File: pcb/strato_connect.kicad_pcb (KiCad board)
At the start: 2 copper layers, 39 parts, among them J1 Conn_Coaxial, J2 Conn_02x03_Odd_Even, SW1 SW_SPST, SW2 SW_SPST, U1 TPS565242, U2 ATmega328PB-A, U4 RF4463F30, Y1 CSTNE16M0V530000R0

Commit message: rough layout of the rev2 pcb
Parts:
- added J3: Conn_01x04_Pin, Connector_JST:JST_SH_SM04B-SRSS-TB_1x04-1MP_P1.00mm_Horizontal, F.Cu at (202.9, 74.3)
- added J4: Conn_01x02_Pin, Connector_JST:JST_PH_S2B-PH-SM4-TB_1x02-1MP_P2.00mm_Horizontal, F.Cu at (219.3, 72.8)
- added J5: Conn_01x05_Pin, Connector_JST:JST_SH_SM05B-SRSS-TB_1x05-1MP_P1.00mm_Horizontal, F.Cu at (203.4, 66.7)
- J2: footprint Connector_PinHeader_2.54mm:PinHeader_2x03_P2.54mm_Vertical -> Connector_PinHeader_2.54mm:PinHeader_2x03_P2.54mm_Vertical_SMD
- U2: value ATmega328PB-A -> ATmega328PB-M; footprint Package_QFP:TQFP-32_7x7mm_P0.8mm -> Package_DFN_QFN:QFN-32-1EP_5x5mm_P0.5mm_EP3.1x3.1mm
- moved U2 36.6 mm to (218.5, 79.5)

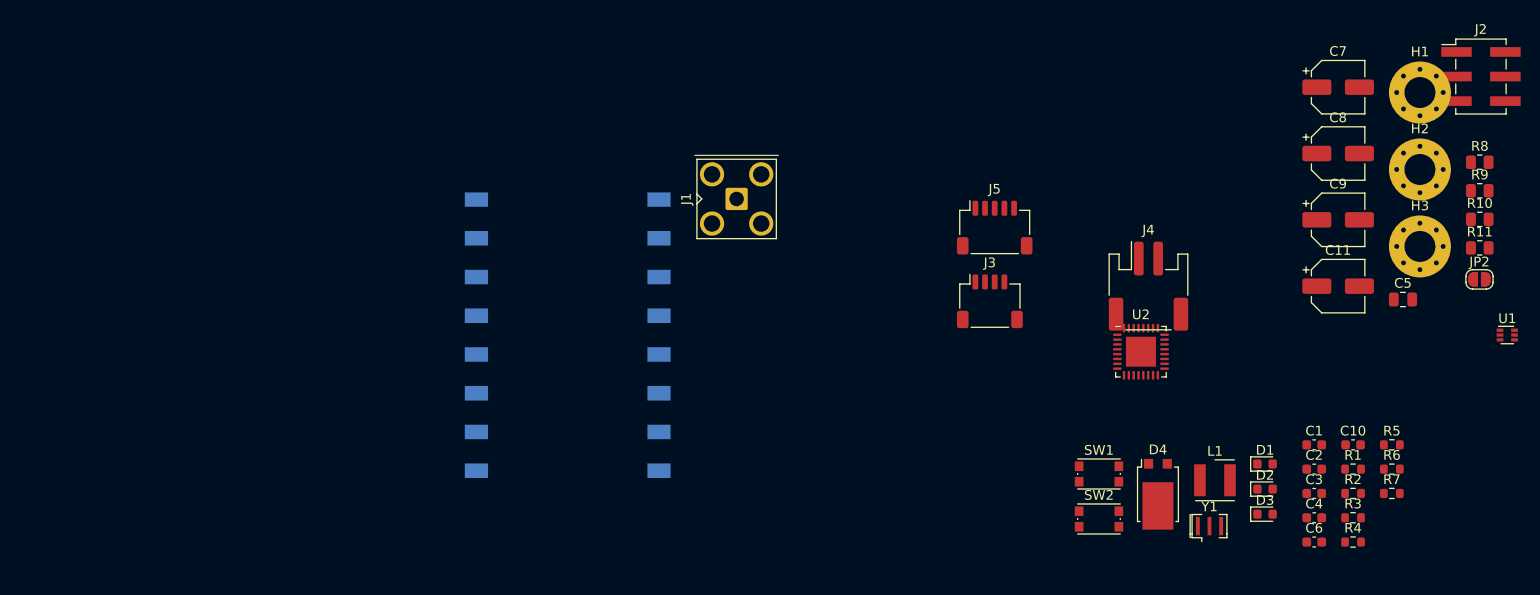
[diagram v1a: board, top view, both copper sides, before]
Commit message: get most of the layout done, need to add some sort of icsp header pins
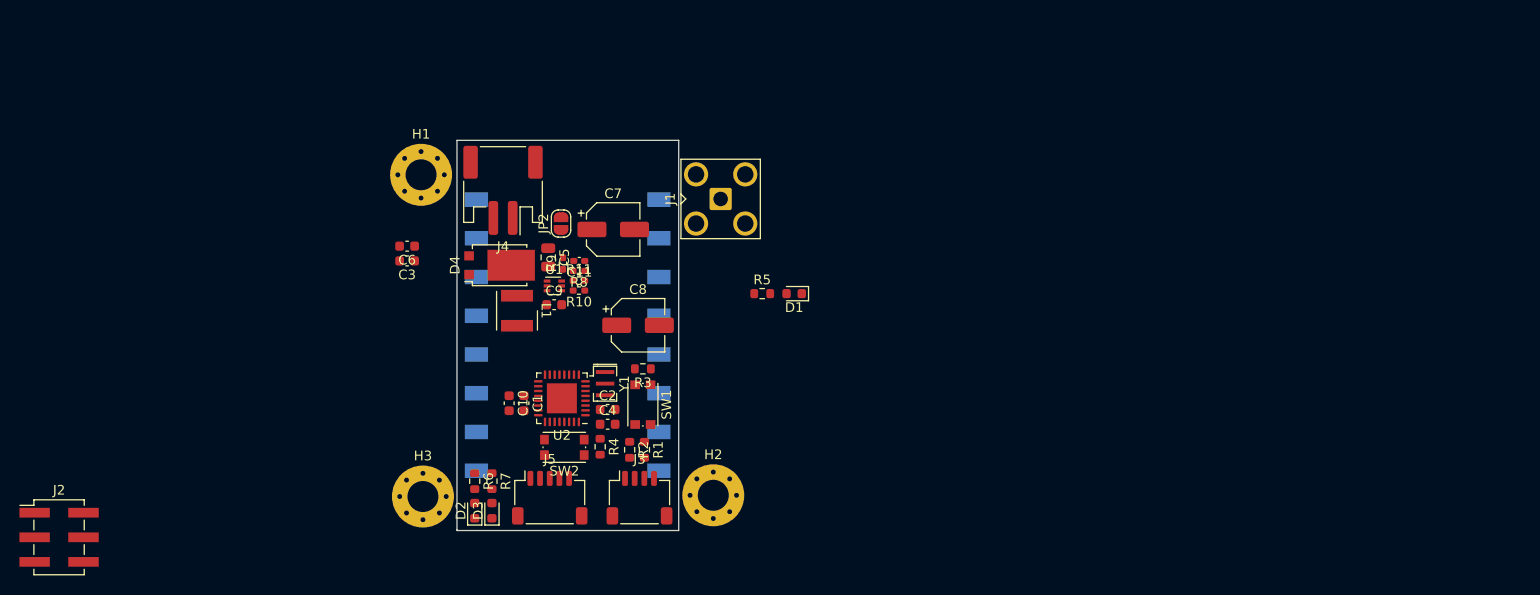
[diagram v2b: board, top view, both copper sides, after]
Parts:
- C11: footprint Capacitor_SMD:CP_Elec_5x5.3 -> Capacitor_SMD:C_0402_1005Metric_Pad0.74x0.62mm_HandSolder
- C9: footprint Capacitor_SMD:CP_Elec_5x5.3 -> Capacitor_SMD:C_0603_1608Metric
- R10, R11, R8, R9: footprint Resistor_SMD:R_0805_2012Metric -> Resistor_SMD:R_0402_1005Metric_Pad0.72x0.64mm_HandSolder
- moved J2 154.4 mm to (106.8, 98.7)
- moved H3 106.2 mm to (144.4, 94.5)
- moved H1 103.5 mm to (144.2, 61.3)
- moved U1 98.6 mm to (158.0, 72.7)
- moved C6 98.5 mm to (142.7, 68.6), turned to 180 degrees
- moved C3 96.7 mm to (142.7, 70.2), turned to 180 degrees
- moved JP2 95.0 mm to (158.6, 66.3), turned to 90 degrees
- moved R9 95.0 mm to (158.8, 70.4), turned to 90 degrees
- moved R6 94.7 mm to (149.7, 92.9), turned to -90 degrees
- moved R8 93.7 mm to (160.5, 71.2), turned to 180 degrees
- moved R10 93.3 mm to (160.5, 73.2), turned to 180 degrees
- moved R11 93.1 mm to (160.5, 72.2)
- moved R7 93.0 mm to (151.5, 92.9), turned to -90 degrees
- moved C5 88.4 mm to (157.3, 69.8), turned to -90 degrees
- moved C10 87.3 mm to (153.3, 84.9), turned to -90 degrees
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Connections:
- C5 pad 1: Net-(D4-K) -> /VDC_FW
- C9 pad 2: Net-(U1-VBST) -> GND
- D4 pad 1: Net-(D4-K) -> /VDC_FW
- R10 pad 1: Net-(D4-K) -> /VDC_FW
- U1 pad 1: GND -> /VDC_FW
- U1 pad 3: Net-(D4-K) -> GND
- U1 pad 4: /FB -> GND
- U1 pad 6: Net-(U1-VBST) -> /FB
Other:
- board outline added: 22.9 x 40.3 mm

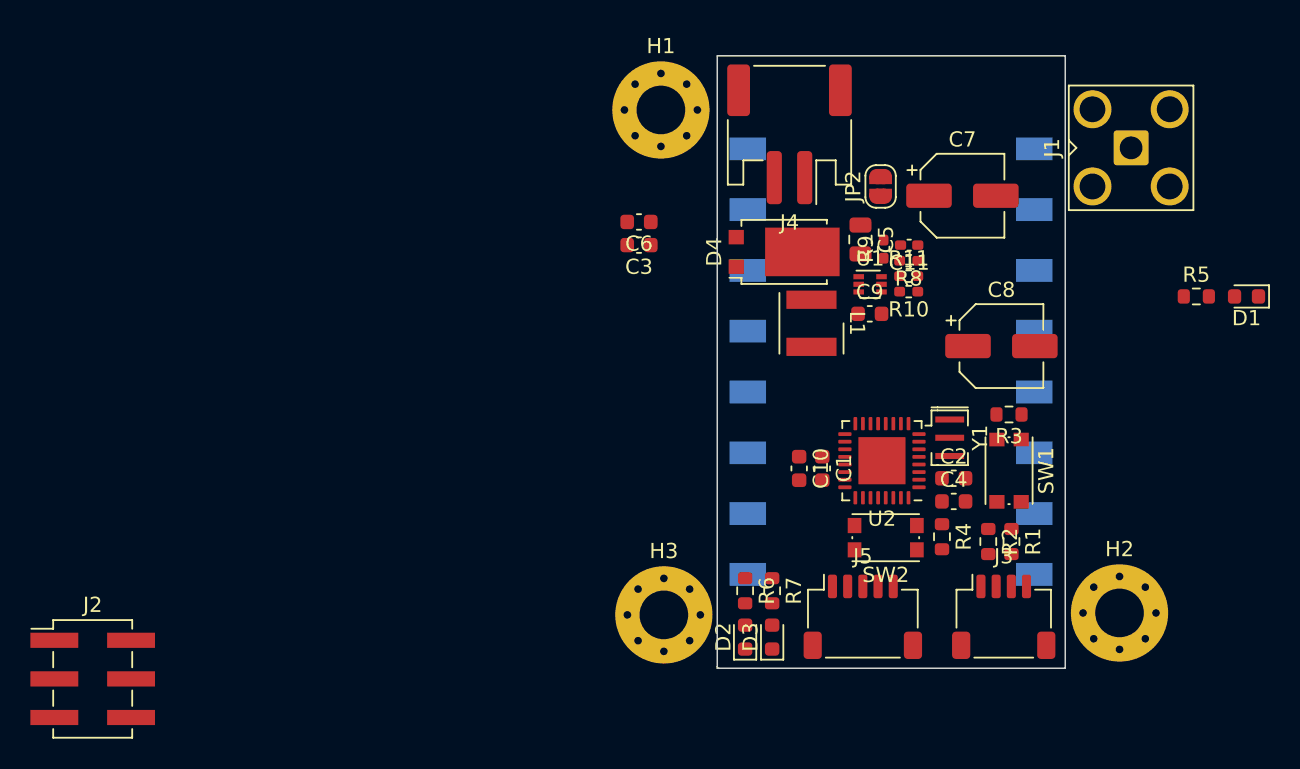
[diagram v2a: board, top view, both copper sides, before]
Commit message: pass DRC with the schematic capture
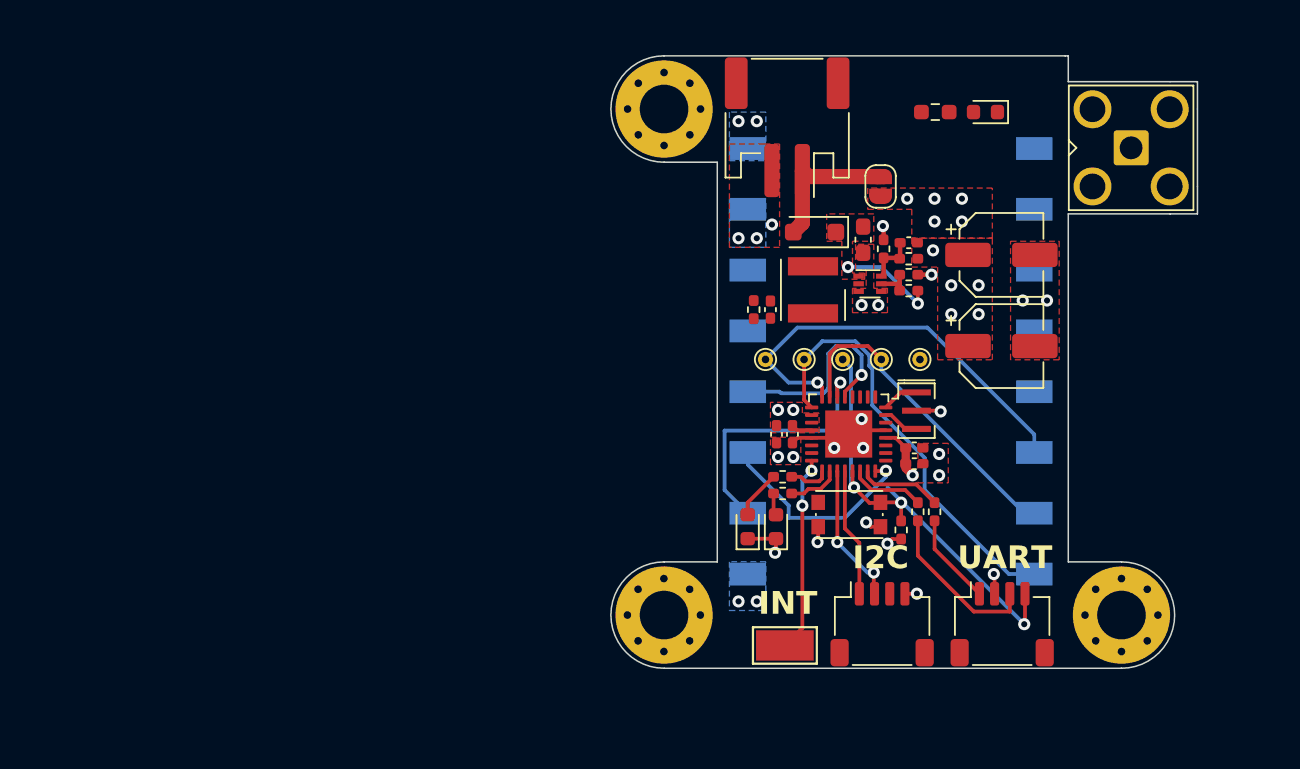
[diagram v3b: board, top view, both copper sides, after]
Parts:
- removed C3: 1u, Capacitor_SMD:C_0603_1608Metric
- removed C6: 100n, Capacitor_SMD:C_0603_1608Metric
- removed R4: 10k, Resistor_SMD:R_0603_1608Metric
- removed SW2: SW_SPST, Button_Switch_SMD:SW_Push_1P1T_NO_CK_KMR2
- added R12: NP, Resistor_SMD:R_0402_1005Metric_Pad0.72x0.64mm_HandSolder, F.Cu at (150.3, 74.4)
- added TP1: TestPoint, TestPoint:TestPoint_THTPad_D1.0mm_Drill0.5mm, F.Cu at (151.1, 77.7)
- added TP2: TestPoint, TestPoint:TestPoint_THTPad_D1.0mm_Drill0.5mm, F.Cu at (153.6, 77.7)
- added TP3: TestPoint, TestPoint:TestPoint_THTPad_D1.0mm_Drill0.5mm, F.Cu at (156.2, 77.7)
- added TP4: TestPoint, TestPoint:TestPoint_THTPad_D1.0mm_Drill0.5mm, F.Cu at (158.7, 77.7)
- added TP5: TestPoint, TestPoint:TestPoint_THTPad_D1.0mm_Drill0.5mm, F.Cu at (161.2, 77.7)
- C1, C10, C2, C4: footprint Capacitor_SMD:C_0603_1608Metric -> Capacitor_SMD:C_0402_1005Metric_Pad0.74x0.62mm_HandSolder
- C5: footprint Capacitor_SMD:C_0805_2012Metric -> Capacitor_SMD:C_0603_1608Metric_Pad1.08x0.95mm_HandSolder
- C9: value 100n -> NP; footprint Capacitor_SMD:C_0603_1608Metric -> Capacitor_SMD:C_0402_1005Metric_Pad0.74x0.62mm_HandSolder
- D4: value ST12199STR -> FS22N; footprint Kevin_Lutzer_Lbr:Diode-TO-277B -> Diode_SMD:D_SOD-123F
- J2: value Conn_02x03_Odd_Even -> Conn_01x04_Pin; footprint Connector_PinHeader_2.54mm:PinHeader_2x03_P2.54mm_Vertical_SMD -> Connector_JST:JST_SH_SM04B-SRSS-TB_1x04-1MP_P1.00mm_Horizontal
- J5: value Conn_01x05_Pin -> Conn_01x01_Pin; footprint Connector_JST:JST_SH_SM05B-SRSS-TB_1x05-1MP_P1.00mm_Horizontal -> TestPoint:TestPoint_Keystone_5019_Minature
- R1, R2, R3, R6, R7: footprint Resistor_SMD:R_0603_1608Metric -> Resistor_SMD:R_0402_1005Metric_Pad0.72x0.64mm_HandSolder
- R5: footprint Resistor_SMD:R_0603_1608Metric -> Resistor_SMD:R_0603_1608Metric_Pad0.98x0.95mm_HandSolder
- moved J2 52.1 mm to (158.8, 95.1)
- moved R5 21.0 mm to (162.2, 61.4)
- moved D1 21.0 mm to (165.6, 61.4)
- moved SW1 10.9 mm to (156.6, 87.9), turned to 180 degrees
- moved R3 10.4 mm to (160.0, 88.9), turned to 90 degrees
- moved R6 7.90 mm to (152.2, 85.4), turned to 180 degrees
- moved D3 7.27 mm to (151.8, 88.7)
- moved D2 7.26 mm to (149.9, 88.7)
- moved C9 6.54 mm to (151.4, 74.4), turned to 90 degrees
- moved R1 6.46 mm to (161.1, 87.7)
- moved R7 6.44 mm to (152.2, 86.5), turned to 180 degrees
- moved J5 5.47 mm to (152.3, 96.5), turned to 180 degrees
- moved C7 4.67 mm to (166.6, 70.8)
- moved R2 4.04 mm to (162.2, 87.7)
- moved C4 3.59 mm to (160.9, 84.5)
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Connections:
- C9 pad 1: /SW -> +5V
- C9 pad 2: GND -> /SW
- J2 pad 1: SPI_MISO -> SCL
- J2 pad 2: +5V -> SDA
- J2 pad 3: SPI_SCK -> unconnected-(J2-Pin_3-Pad3)
- J2 pad 4: SPI_MOSI -> GND
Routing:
- net ~{RST}: track 0.00 -> 29.3 mm, vias 0 -> 3
- net SPI_SCK: track 0.00 -> 28.4 mm
- net SPI_MISO: track 0.00 -> 27.8 mm, vias 0 -> 1
- net SPI_MOSI: track 0.00 -> 21.5 mm
- net ~{SPI_CS}: track 0.00 -> 17.7 mm, vias 0 -> 1
- net GND: track 0.00 -> 16.9 mm, vias 0 -> 24
- net ~{IRQ}: track 0.00 -> 14.0 mm, vias 0 -> 1
- net ~{SDN}: track 0.00 -> 13.6 mm, vias 0 -> 1
- net ~{INT}: track 0.00 -> 12.9 mm, vias 0 -> 2
- net UART_RX: track 0.00 -> 11.0 mm
- net VDC: track 0.00 -> 9.61 mm
- net SDA: track 0.00 -> 9.33 mm, vias 0 -> 2
- net SCL: track 0.00 -> 8.47 mm
- net /VDC_FW: track 0.00 -> 6.45 mm, vias 0 -> 2
- net UART_TX: track 0.00 -> 6.02 mm
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- added copper zone on B.Cu, net +5V
- added copper zone on F.Cu, net +5V
- added copper zone on In1.Cu, net +5V
- added copper zone on F.Cu, net /VDC_FW
- added copper zone on B.Cu, net GND
- added copper zone on F.Cu, net GND
- added copper zone on In2.Cu, net GND
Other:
- board size 22.9 x 40.3 mm -> 38.6 x 40.3 mm
- copper layers 2 -> 4
- board text added: "I2C"
- board text added: "INT"
- board text added: "UART"

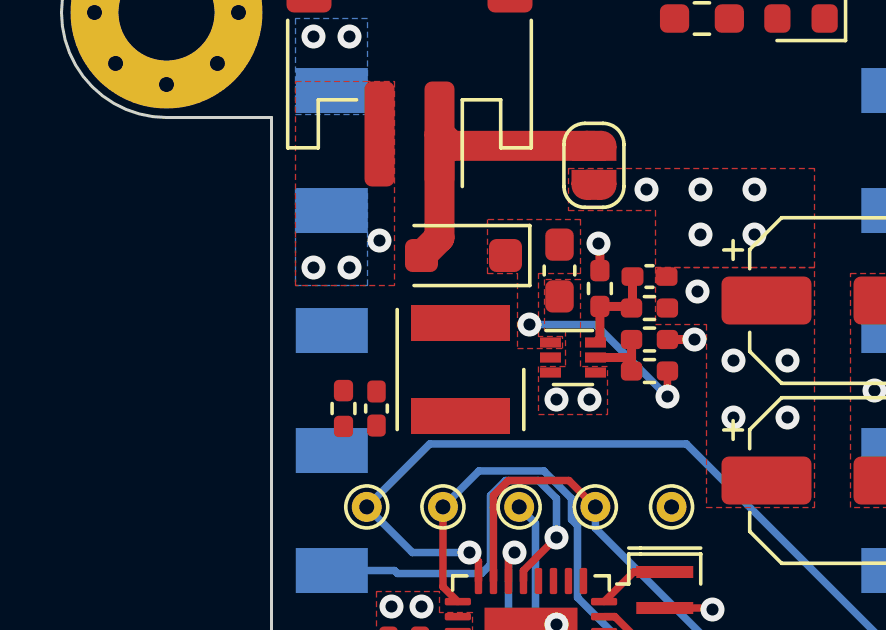
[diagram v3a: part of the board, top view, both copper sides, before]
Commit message: add the 4025 Weurth inductor footprint in
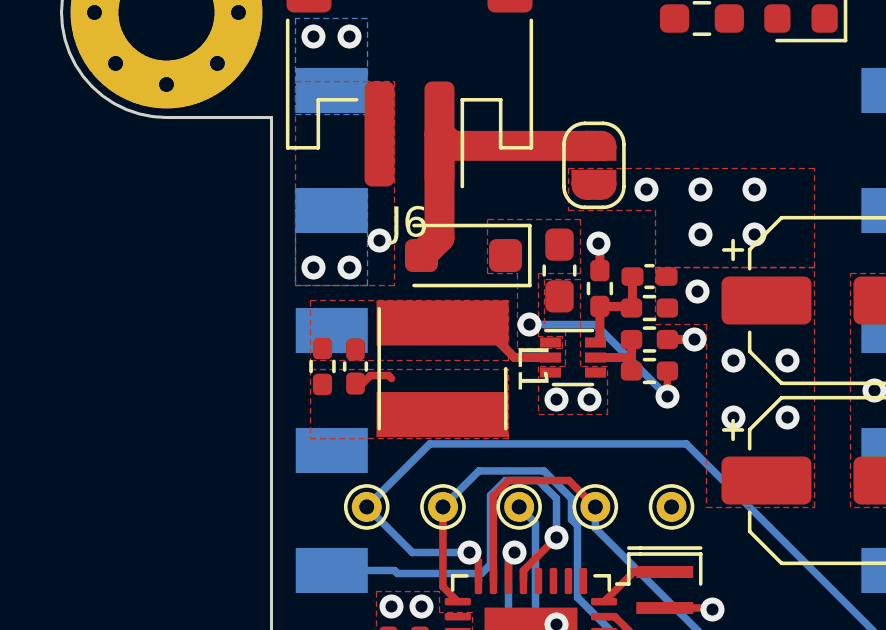
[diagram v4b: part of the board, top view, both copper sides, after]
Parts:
- removed J4: Conn_01x02_Pin, Connector_JST:JST_PH_S2B-PH-SM4-TB_1x02-1MP_P2.00mm_Horizontal
- added J6: Conn_01x02_Pin, Connector_JST:JST_PH_S2B-PH-SM4-TB_1x02-1MP_P2.00mm_Horizontal, F.Cu at (152.5, 62.4)
- L1: footprint Inductor_SMD_Wurth:L_Wurth_WE-LQSH-4020 -> Kevin_Lutzer_Lbr:L_Wurth_WE-LQSH-4025
- moved C9 1.57 mm to (150.7, 73.0)
- moved R12 1.57 mm to (149.6, 73.0)
- moved L1 0.60 mm to (153.6, 73.1)
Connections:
- U2 pad 1: ~{TRIG} -> unconnected-(U2-PD3-Pad1)
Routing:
- net /SW: track 0.00 -> 4.08 mm
- net +5V: track 5.99 -> 7.34 mm
- added copper zone on F.Cu, net /SW

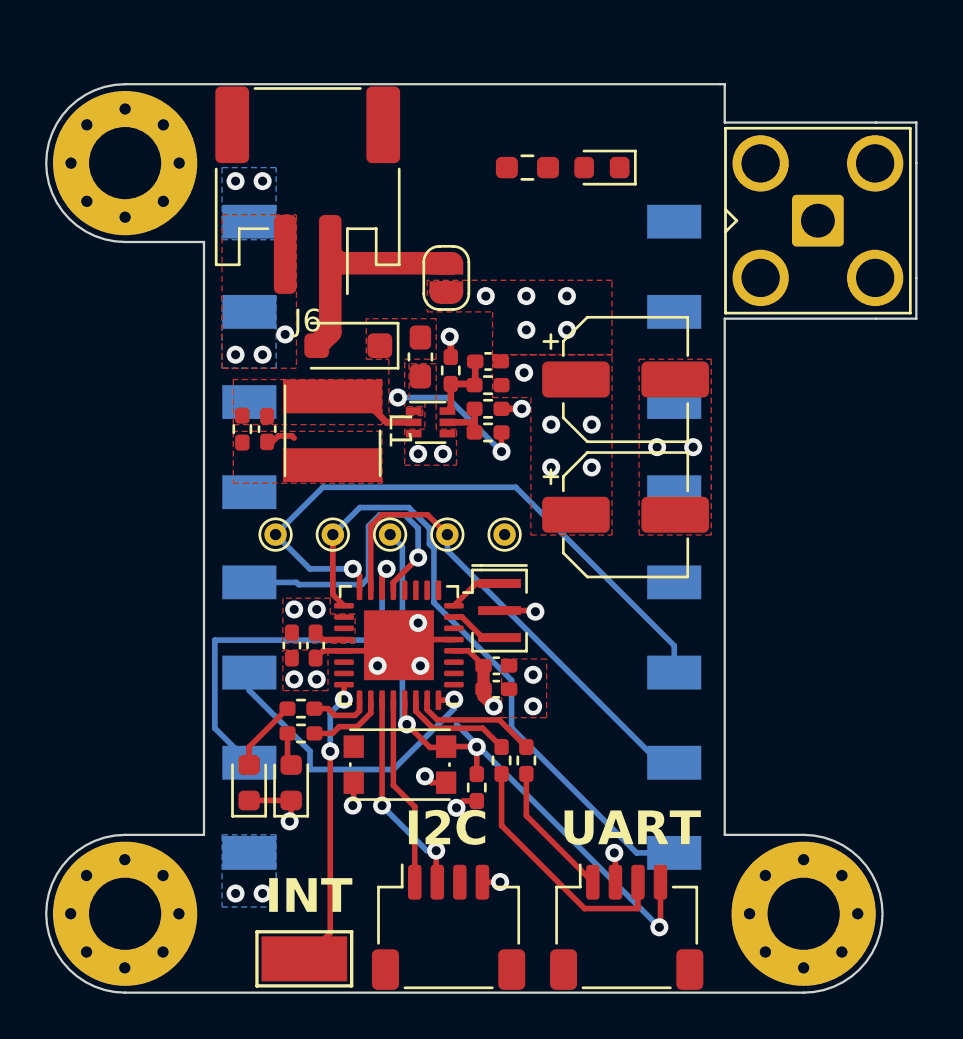
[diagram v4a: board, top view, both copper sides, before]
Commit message: pass drc rules for files, just have to add the silk screen
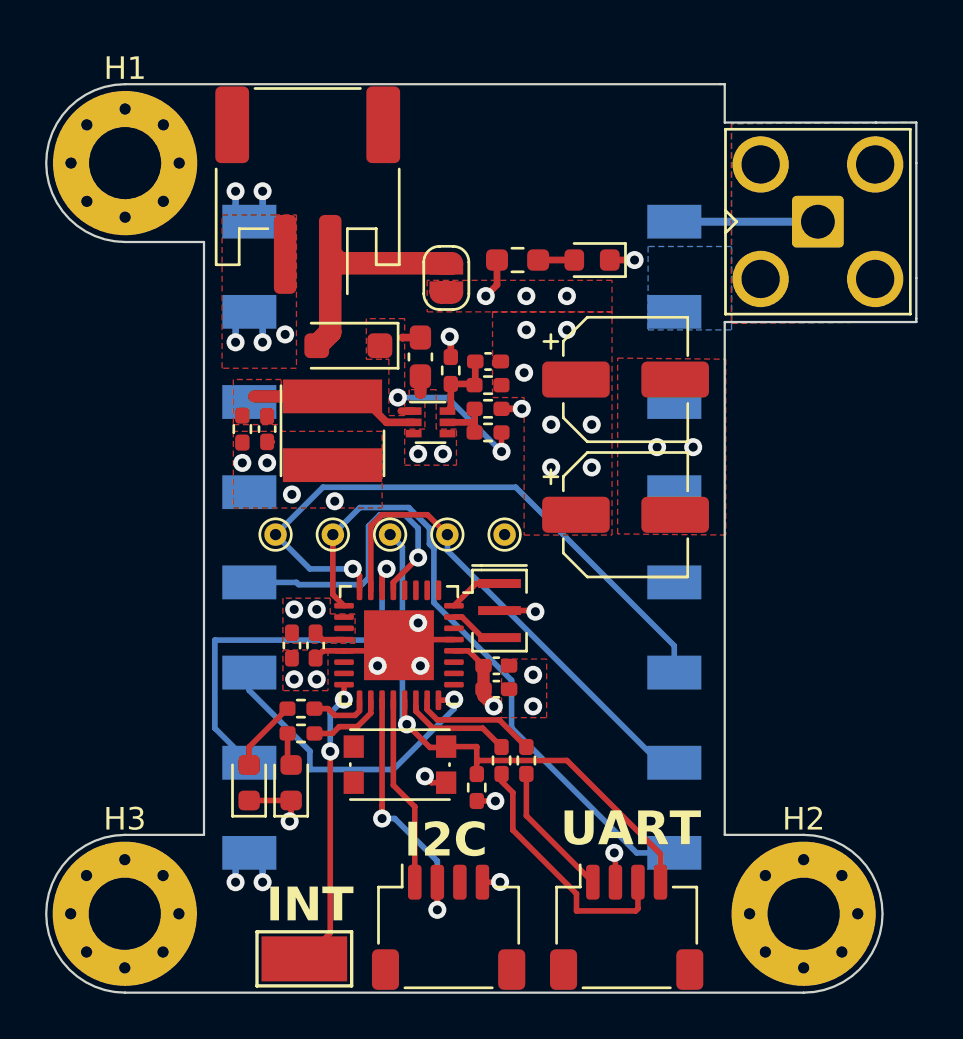
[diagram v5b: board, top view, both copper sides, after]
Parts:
- moved D1 4.12 mm to (165.1, 65.5)
- moved R5 4.12 mm to (161.8, 65.5)
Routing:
- net Net-(J1-In): track 0.00 -> 6.37 mm
- net GND: track 16.9 -> 21.7 mm
- net ~{RST}: track 29.3 -> 25.7 mm, vias 3 -> 1
- net /SW: track 4.08 -> 7.55 mm
- net +5V: track 7.34 -> 10.2 mm, vias 16 -> 20
- net SDA: track 9.33 -> 11.9 mm
- net Net-(D1-A): track 0.00 -> 1.60 mm
- net /VDC_FW: track 6.45 -> 7.80 mm
- net Net-(U2-XTAL1/PB6): track 2.40 -> 1.65 mm
- net SPI_MOSI: track 21.5 -> 20.8 mm
- added copper zone on B.Cu, net /RF_GND
- added copper zone on F.Cu, net /RF_GND
- added copper zone on In1.Cu, net /RF_GND
- added copper zone on In2.Cu, net /RF_GND
- removed copper zone on B.Cu, net +5V
- removed copper zone on B.Cu, net GND
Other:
- outline, holes or cut-outs redrawn

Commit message: finish the design
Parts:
- added kibuzzard-64B1A828: G***, kibuzzard-64B1A828, F.Cu at (166.6, 91.2)
- added kibuzzard-64B1A87B: G***, kibuzzard-64B1A87B, F.Cu at (158.8, 91.2)
- added kibuzzard-64B1A895: G***, kibuzzard-64B1A895, F.Cu at (152.3, 93.8)
- added kibuzzard-64B1B5E1: G***, kibuzzard-64B1B5E1, F.Cu at (163.2, 61.6)
- added kibuzzard-64B1B6FD: G***, kibuzzard-64B1B6FD, F.Cu at (166.7, 82.3)
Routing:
- net UART_RX: track 11.4 -> 8.77 mm
- net GND: track 21.7 -> 21.4 mm, vias 24 -> 23
- net (no net): vias 0 -> 1
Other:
- board text added: "For colplanar: 0.777mm trace width 0.15mm spacing"
- board text removed: "I2C"
- board text removed: "INT"
- board text removed: "UART"
